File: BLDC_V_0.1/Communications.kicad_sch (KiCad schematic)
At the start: 42 parts, among them J12 Conn_01x03, J4 Conn_01x04, J8 15EDGVC-3.5-03P-14-00AH, J9 Conn_01x05, J9 Conn_01x06, U11 ISO1050DUB, U8 B0505S-1WR2

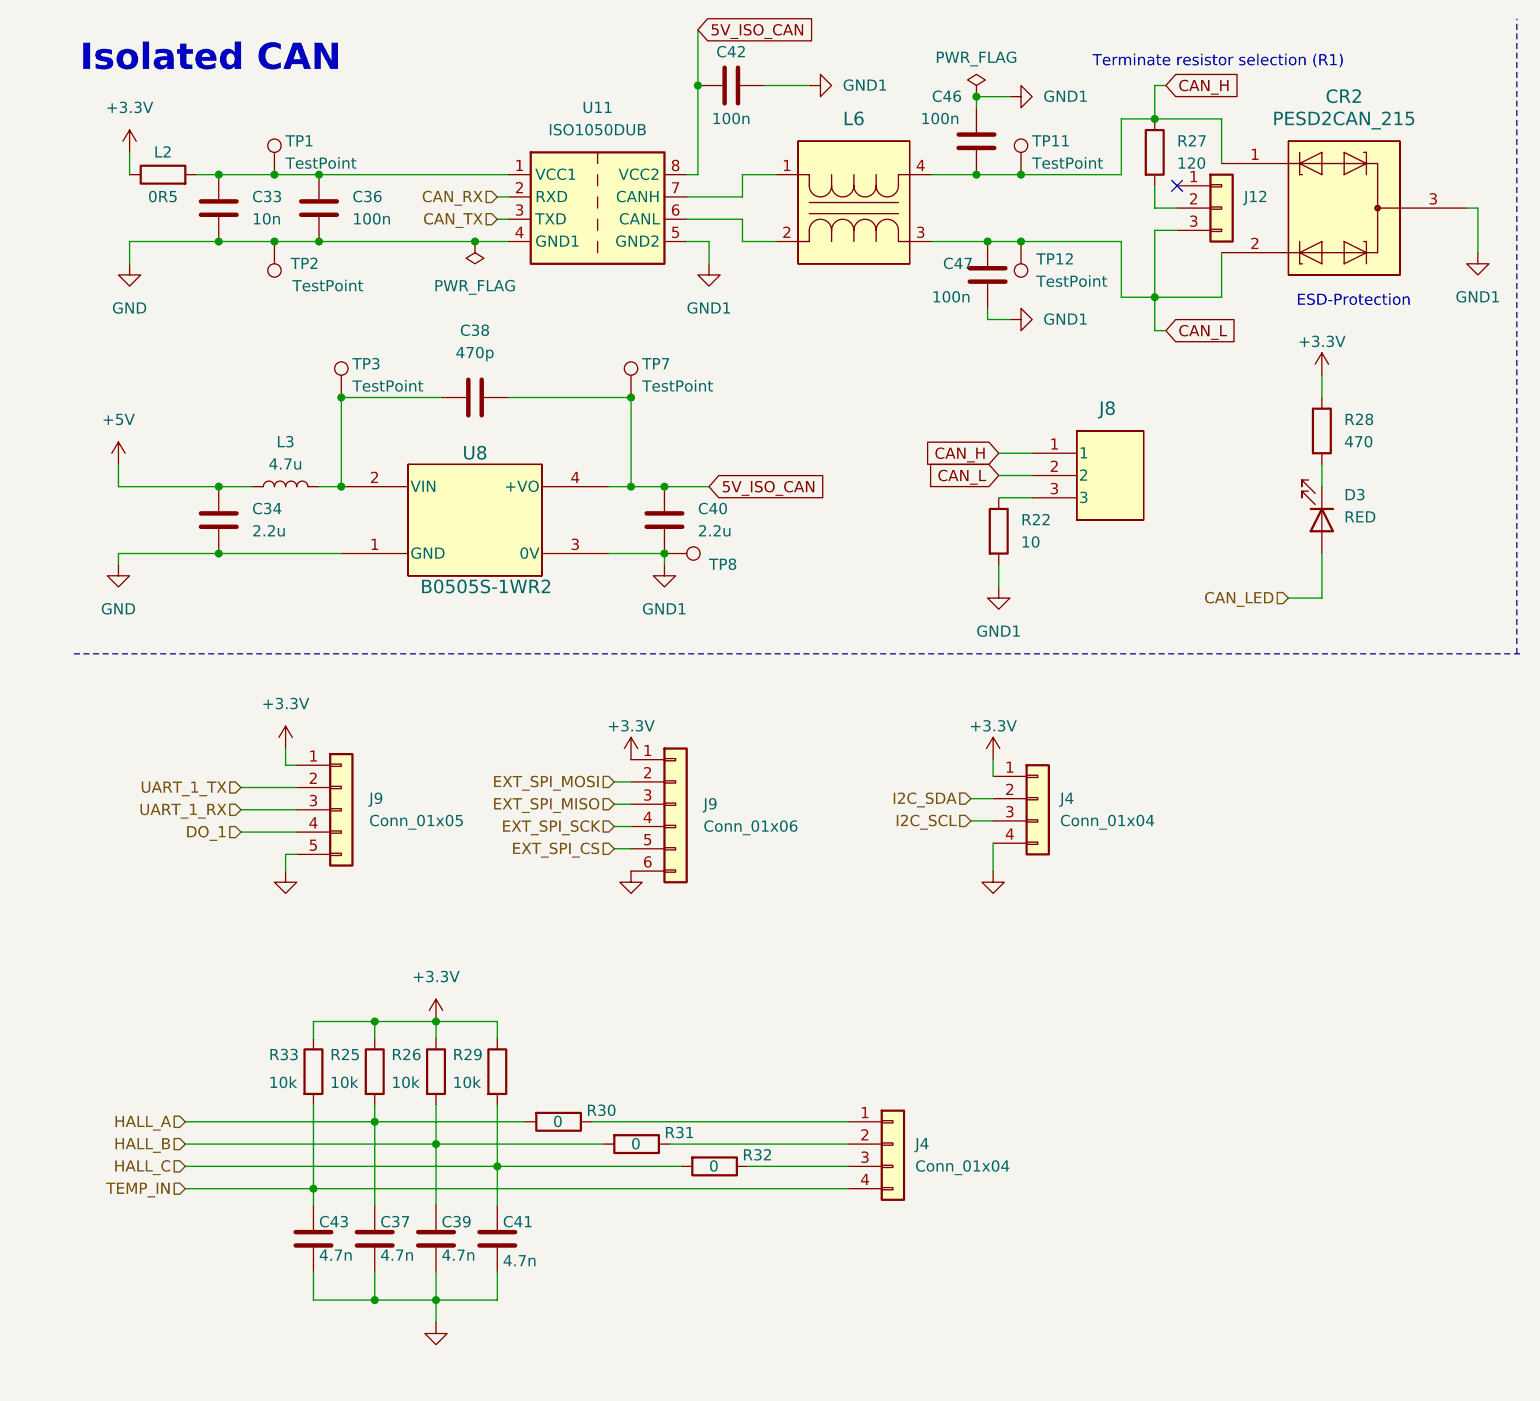
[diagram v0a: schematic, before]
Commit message: Schematic prototip done.
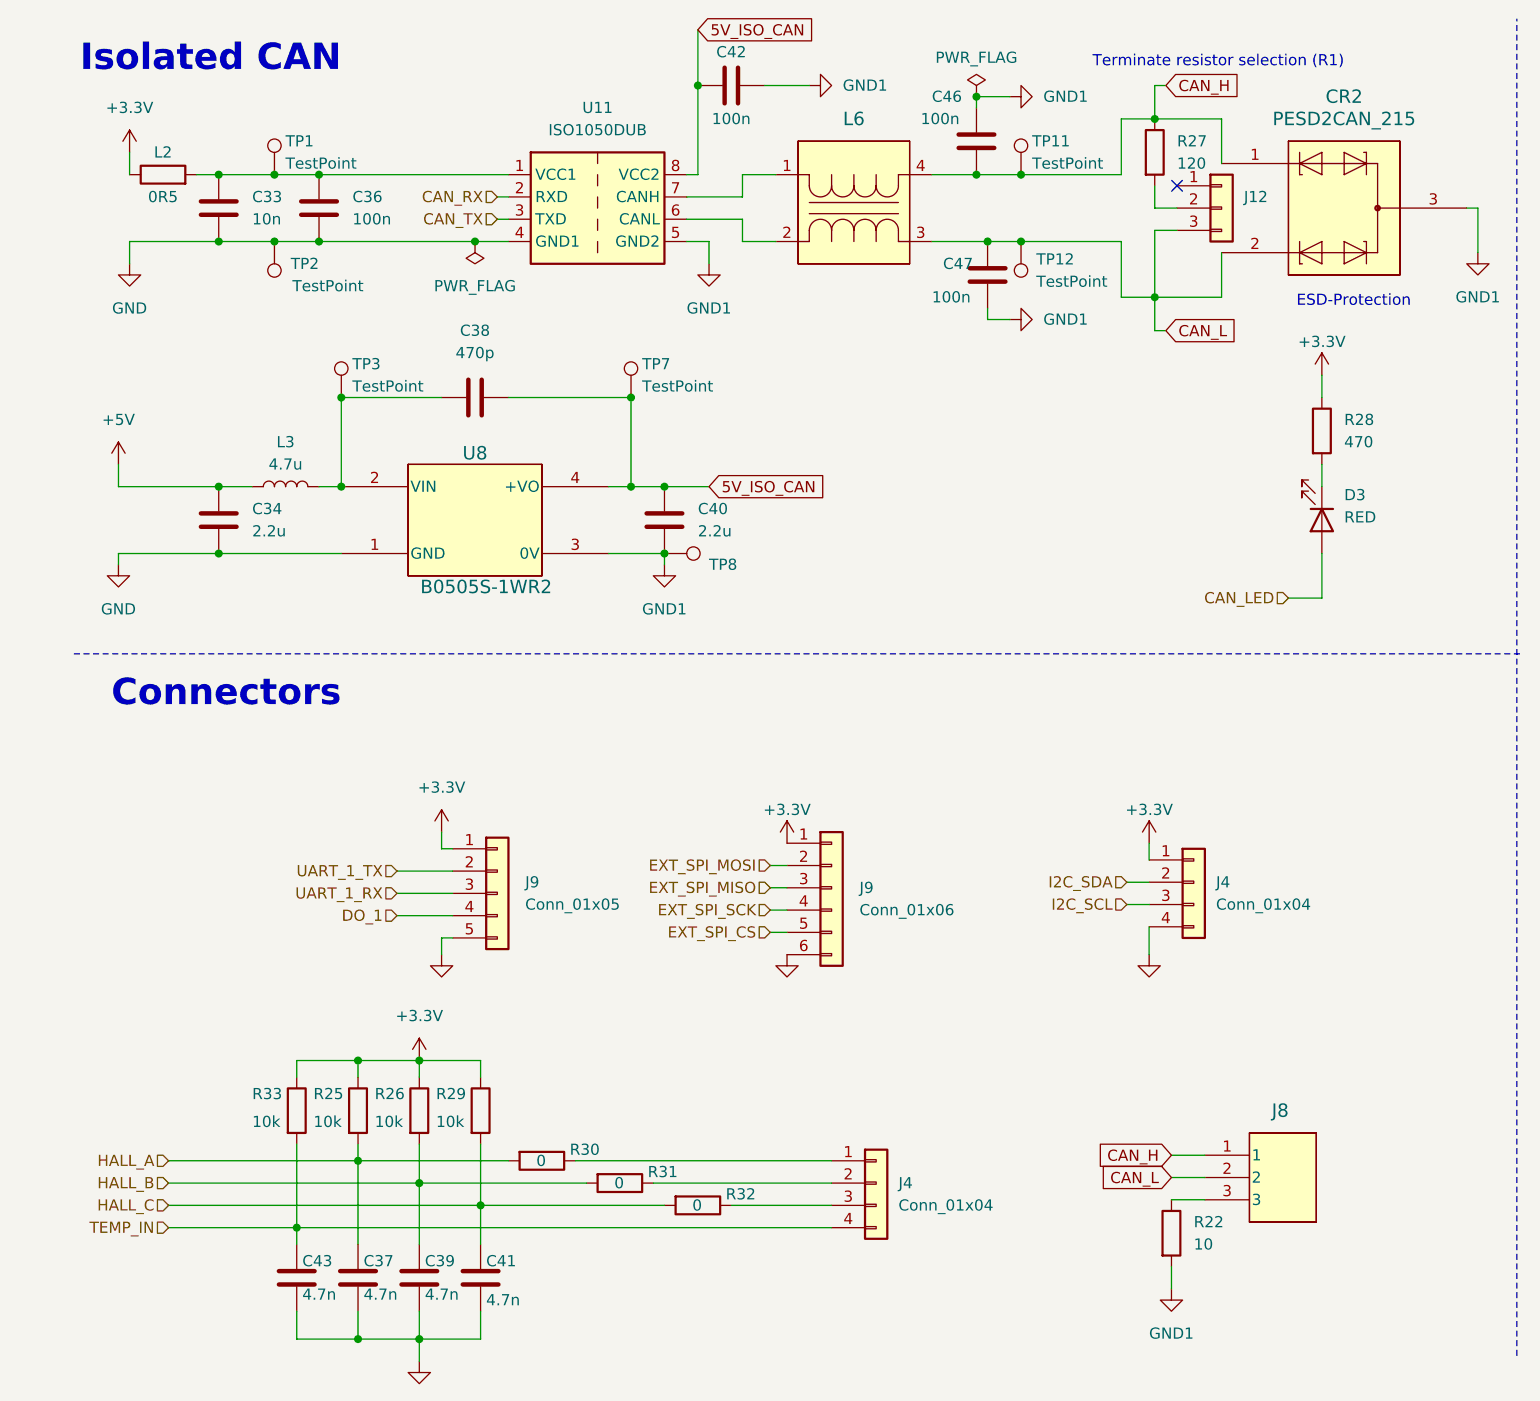
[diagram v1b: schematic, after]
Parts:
- C37, C39, C41, C43: footprint (none) -> Capacitor_SMD:C_0402_1005Metric
- R25, R26, R29, R30, R31, R32, R33: footprint (none) -> Resistor_SMD:R_0603_1608Metric
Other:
- note added: "Connectors"
- moved on the sheet: C37, C39, C41, C43, J4, J8, J9, R22, R25, R26, R29, R30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

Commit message: PCB placement completed.
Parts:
- removed TP11, TP12: TestPoint, TestPoint:TestPoint_Loop_D1.80mm_Drill1.0mm_Beaded, symbol Connector:TestPoint
- J12: footprint Connector_JST:JST_EH_S3B-EH_1x03_P2.50mm_Horizontal -> Connector_PinHeader_2.54mm:PinHeader_1x03_P2.54mm_Vertical
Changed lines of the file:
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@@
   (junction (at 75.565 66.675) (diameter 0) (color 0 0 0 0)
   )
-  (junction (at 120.015 31.115) (diameter 0) (color 0 0 0 0)
-  )
   (junction (at 57.785 38.735) (diameter 0) (color 0 0 0 0)
   )
@@
   )
   (junction (at 114.935 22.225) (diameter 0) (color 0 0 0 0)
-  )
-  (junction (at 120.015 38.735) (diameter 0) (color 0 0 0 0)
   )
   (junction (at 51.435 163.83) (diameter 0) (color 0 0 0 0)
@@
     (stroke (width 0) (type default))
   )
-  (wire (pts (xy 120.015 38.735) (xy 131.445 38.735))
+  (wire (pts (xy 116.205 38.735) (xy 131.445 38.735))
     (stroke (width 0) (type default))
   )
@@
     (stroke (width 0) (type default))
   )
-  (wire (pts (xy 120.015 31.115) (xy 131.445 31.115))
+  (wire (pts (xy 114.935 31.115) (xy 131.445 31.115))
     (stroke (width 0) (type default))
   )
@@
   )
   (wire (pts (xy 22.86 151.13) (xy 37.465 151.13))
-    (stroke (width 0) (type default))
-  )
-  (wire (pts (xy 114.935 31.115) (xy 120.015 31.115))
     (stroke (width 0) (type default))
   )
@@
   )
   (wire (pts (xy 88.265 38.735) (xy 92.075 38.735))
-    (stroke (width 0) (type default))
-  )
-  (wire (pts (xy 120.015 38.735) (xy 116.205 38.735))
     (stroke (width 0) (type default))
   )
@@
     )
   )
-  (symbol (lib_id "Connector:TestPoint") (at 120.015 38.735 180) (unit 1)
-    (in_bom yes) (on_board yes) (dnp no) (fields_autoplaced)
-    (property "Reference" "TP12" (at 121.7617 40.767 0)
-      (effects (font (size 1.27 1.27)) (justify right))
-    )
-    (property "Value" "TestPoint" (at 121.7617 43.307 0)
-      (effects (font (size 1.27 1.27)) (justify right))
-    )
-    (property "Footprint" "TestPoint:TestPoint_Loop_D1.80mm_Drill1.0mm_Beaded" (at 114.935 38.735 0)
-      (effects (font (size 1.27 1.27)) hide)
-    )
-    (property "Datasheet" "~" (at 114.935 38.735 0)
-      (effects (font (size 1.27 1.27)) hide)
-    )
-    (pin "1")
-    (instances
-      (project "BLDC_V_0.1"
-        (path "/4cd36721-3778-4ad1-9865-468b6186ee19/0b08cf2e-adc1-43e0-b092-2bca45900a22"
-          (reference "TP12") (unit 1)
-        )
-      )
-      (project "CAN_2x_485"
-        (path "/71e8aef5-e069-41ad-a908-5bfc657219c6"
-          (reference "TP2") (unit 1)
-        )
-      )
-    )
-  )
   (symbol (lib_id "Device:R") (at 135.255 28.575 0) (unit 1)
     (in_bom yes) (on_board yes) (dnp no) (fields_autoplaced)
@@
       (effects (font (size 1.27 1.27)) (justify left) hide)
     )
-    (property "Footprint" "Connector_JST:JST_EH_S3B-EH_1x03_P2.50mm_Horizontal" (at 142.875 34.925 0)
+    (property "Footprint" "Connector_PinHeader_2.54mm:PinHeader_1x03_P2.54mm_Vertical" (at 142.875 34.925 0)
       (effects (font (size 1.27 1.27)) hide)
     )
@@
         )
       )
-    )
-  )
-  (symbol (lib_id "Connector:TestPoint") (at 120.015 31.115 0) (unit 1)
-    (in_bom yes) (on_board yes) (dnp no)
-    (property "Reference" "TP11" (at 121.285 27.305 0)
-      (effects (font (size 1.27 1.27)) (justify left))
-    )
-    (property "Value" "TestPoint" (at 121.285 29.845 0)
-      (effects (font (size 1.27 1.27)) (justify left))
-    )
-    (property "Footprint" "TestPoint:TestPoint_Loop_D1.80mm_Drill1.0mm_Beaded" (at 125.095 31.115 0)
-      (effects (font (size 1.27 1.27)) hide)
-    )
-    (property "Datasheet" "~" (at 125.095 31.115 0)
-      (effects (font (size 1.27 1.27)) hide)
-    )
-    (pin "1")
-    (instances
-      (project "BLDC_V_0.1"
-        (path "/4cd36721-3778-4ad1-9865-468b6186ee19/0b08cf2e-adc1-43e0-b092-2bca45900a22"
-          (reference "TP11") (unit 1)
-        )
-      )
-      (project "CAN_2x_485"
-        (path "/71e8aef5-e069-41ad-a908-5bfc657219c6"
-          (reference "TP1") (unit 1)
-        )
-      )
